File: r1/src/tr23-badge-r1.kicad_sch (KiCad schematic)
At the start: 60 parts, among them Q1 MMBT3904-TP, Q2 MMBT3904-TP, Q3 MMBT3904-TP, Y1 32.768kHz

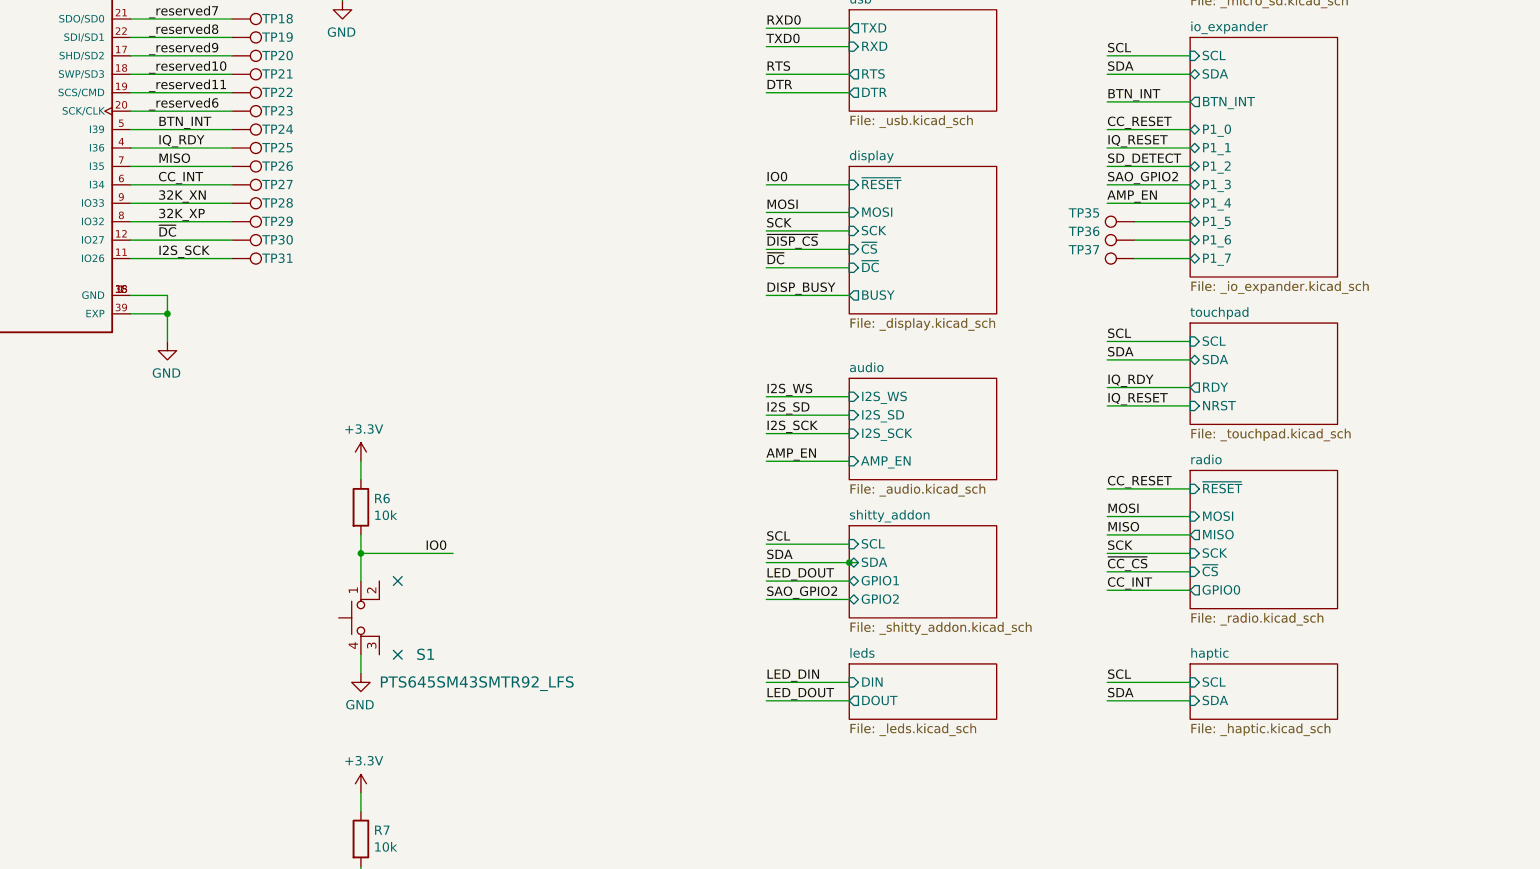
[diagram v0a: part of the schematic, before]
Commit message: Delete haptic and touchpad modules
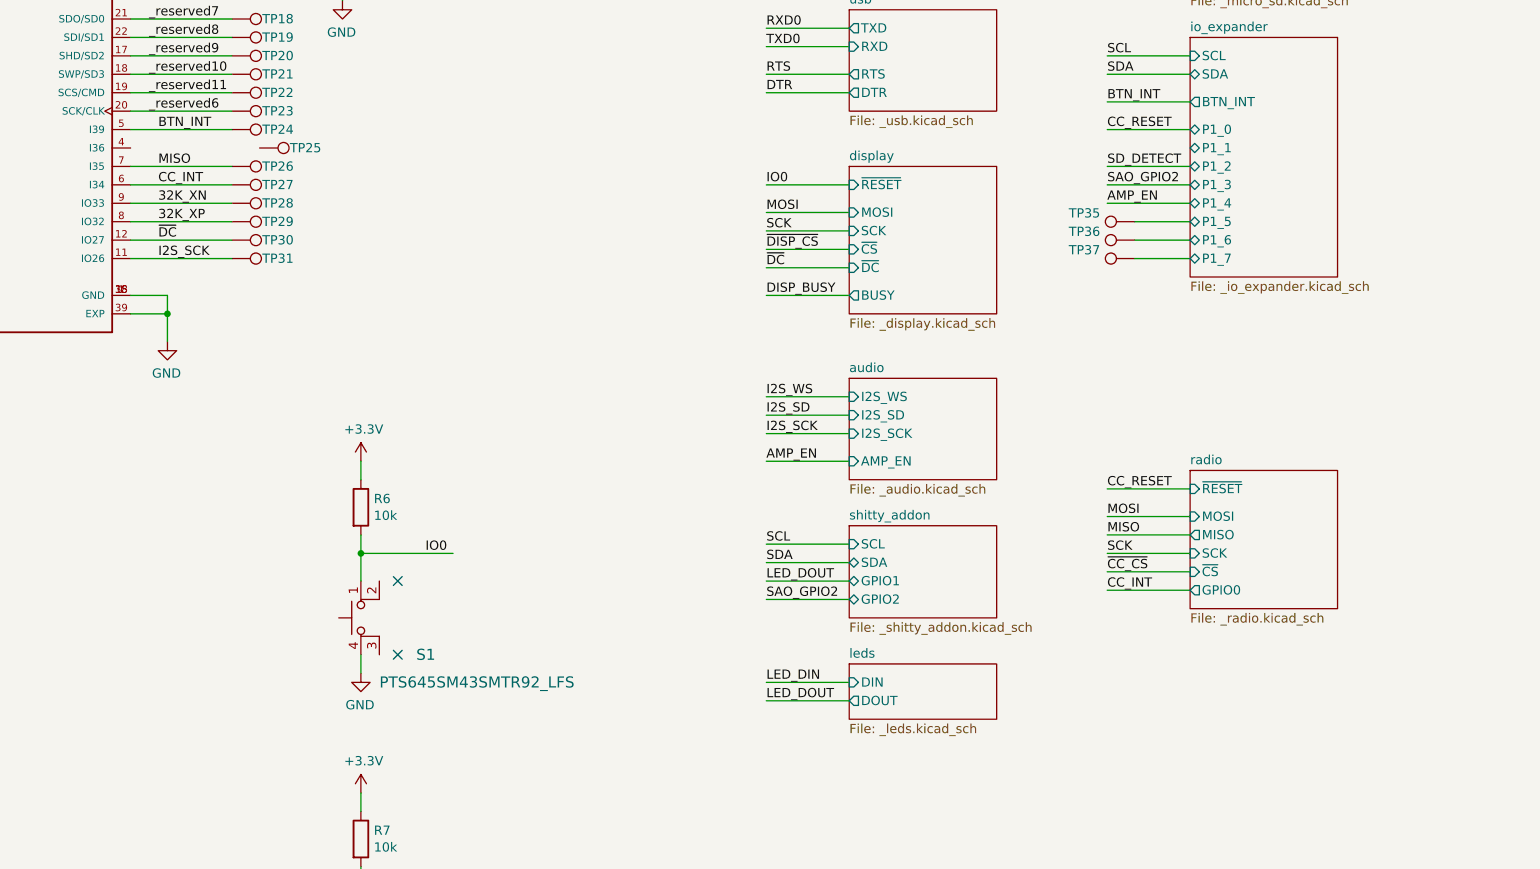
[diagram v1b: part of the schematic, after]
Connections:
- net IQ_RDY: no longer names the net of A1.4 (I36)
- net IQ_RDY: no longer TP25.1
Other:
- removed sheet haptic
- removed sheet touchpad
- moved on the sheet: TP25
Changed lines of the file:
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@@
   (junction (at 125.73 34.29) (diameter 0) (color 0 0 0 0)
-  )
-  (junction (at 195.58 124.46) (diameter 0) (color 0 0 0 0)
   )
   (junction (at 36.83 132.08) (diameter 0) (color 0 0 0 0)
@@
     (stroke (width 0) (type default))
   )
-  (wire (pts (xy 196.85 124.46) (xy 195.58 124.46))
+  (wire (pts (xy 184.15 124.46) (xy 195.58 124.46))
     (stroke (width 0) (type default))
   )
@@
     (stroke (width 0) (type default))
   )
-  (wire (pts (xy 231.14 102.87) (xy 242.57 102.87))
-    (stroke (width 0) (type default))
-  )
   (wire (pts (xy 242.57 77.47) (xy 234.95 77.47))
     (stroke (width 0) (type default))
@@
     (stroke (width 0) (type default))
   )
-  (wire (pts (xy 242.57 140.97) (xy 231.14 140.97))
-    (stroke (width 0) (type default))
-  )
   (wire (pts (xy 231.14 38.1) (xy 242.57 38.1))
     (stroke (width 0) (type default))
@@
     (stroke (width 0) (type default))
   )
-  (wire (pts (xy 96.52 67.31) (xy 110.49 67.31))
-    (stroke (width 0) (type default))
-  )
   (wire (pts (xy 128.27 179.07) (xy 128.27 185.42))
     (stroke (width 0) (type default))
@@
     (stroke (width 0) (type default))
   )
-  (wire (pts (xy 231.14 100.33) (xy 242.57 100.33))
-    (stroke (width 0) (type default))
-  )
   (wire (pts (xy 96.52 49.53) (xy 110.49 49.53))
     (stroke (width 0) (type default))
@@
     (stroke (width 0) (type default))
   )
-  (wire (pts (xy 231.14 96.52) (xy 242.57 96.52))
-    (stroke (width 0) (type default))
-  )
   (wire (pts (xy 66.04 77.47) (xy 52.07 77.47))
     (stroke (width 0) (type default))
@@
     (stroke (width 0) (type default))
   )
-  (wire (pts (xy 242.57 93.98) (xy 231.14 93.98))
-    (stroke (width 0) (type default))
-  )
-  (wire (pts (xy 242.57 67.31) (xy 231.14 67.31))
-    (stroke (width 0) (type default))
-  )
   (wire (pts (xy 34.29 115.57) (xy 39.37 115.57))
     (stroke (width 0) (type default))
@@
     (stroke (width 0) (type default))
   )
-  (wire (pts (xy 195.58 124.46) (xy 184.15 124.46))
-    (stroke (width 0) (type default))
-  )
   (wire (pts (xy 195.58 101.6) (xy 184.15 101.6))
     (stroke (width 0) (type default))
@@
     (stroke (width 0) (type default))
   )
-  (wire (pts (xy 242.57 143.51) (xy 231.14 143.51))
-    (stroke (width 0) (type default))
-  )
   (wire (pts (xy 242.57 64.77) (xy 231.14 64.77))
     (stroke (width 0) (type default))
@@
     (effects (font (size 1.27 1.27)) (justify left bottom))
   )
-  (label "IQ_RDY" (at 100.33 67.31 0)
-    (effects (font (size 1.27 1.27)) (justify left bottom))
-  )
   (label "MOSI" (at 231.14 118.11 0)
     (effects (font (size 1.27 1.27)) (justify left bottom))
@@
     (effects (font (size 1.27 1.27)) (justify left bottom))
   )
-  (label "IQ_RESET" (at 231.14 102.87 0)
-    (effects (font (size 1.27 1.27)) (justify left bottom))
-  )
   (label "~{CC_CS}" (at 52.07 74.93 0)
     (effects (font (size 1.27 1.27)) (justify left bottom))
@@
     (effects (font (size 1.27 1.27)) (justify left bottom))
   )
-  (label "SDA" (at 231.14 143.51 0)
-    (effects (font (size 1.27 1.27)) (justify left bottom))
-  )
   (label "_reserved11" (at 99.06 59.69 0)
     (effects (font (size 1.27 1.27)) (justify left bottom))
@@
     (effects (font (size 1.27 1.27)) (justify left bottom))
   )
-  (label "SDA" (at 231.14 96.52 0)
-    (effects (font (size 1.27 1.27)) (justify left bottom))
-  )
   (label "SCL" (at 184.15 121.92 0)
     (effects (font (size 1.27 1.27)) (justify left bottom))
@@
     (effects (font (size 1.27 1.27)) (justify left bottom))
   )
-  (label "IQ_RDY" (at 231.14 100.33 0)
-    (effects (font (size 1.27 1.27)) (justify left bottom))
-  )
   (label "SCK" (at 52.07 69.85 0)
     (effects (font (size 1.27 1.27)) (justify left bottom))
@@
     (effects (font (size 1.27 1.27)) (justify left bottom))
   )
-  (label "SCL" (at 231.14 140.97 0)
-    (effects (font (size 1.27 1.27)) (justify left bottom))
-  )
   (label "AMP_EN" (at 231.14 74.93 0)
     (effects (font (size 1.27 1.27)) (justify left bottom))
@@
     (effects (font (size 1.27 1.27)) (justify left bottom))
   )
-  (label "SCL" (at 231.14 93.98 0)
-    (effects (font (size 1.27 1.27)) (justify left bottom))
-  )
   (label "SCL" (at 52.07 57.15 0)
     (effects (font (size 1.27 1.27)) (justify left bottom))
@@
   )
   (label "I2S_WS" (at 52.07 59.69 0)
-    (effects (font (size 1.27 1.27)) (justify left bottom))
-  )
-  (label "IQ_RESET" (at 231.14 67.31 0)
     (effects (font (size 1.27 1.27)) (justify left bottom))
   )
@@
     )
   )
-  (symbol (lib_id "Connector:TestPoint") (at 110.49 67.31 270) (unit 1)
-    (in_bom yes) (on_board yes) (dnp no)
-    (property "Reference" "TP25" (at 116.84 67.31 90)
-      (effects (font (size 1.27 1.27)))
-    )
-    (property "Value" "~" (at 112.3696 69.9516 90)
-      (effects (font (size 1.27 1.27)) hide)
-    )
-    (property "Footprint" "jeffmakes-footprints:test-pad-1.4-TH" (at 110.49 72.39 0)
-      (effects (font (size 1.27 1.27)) hide)
-    )
-    (property "Datasheet" "~" (at 110.49 72.39 0)
+  (symbol (lib_id "Connector:TestPoint") (at 114.3 67.31 270) (unit 1)
+    (in_bom yes) (on_board yes) (dnp no)
+    (property "Reference" "TP25" (at 120.65 67.31 90)
+      (effects (font (size 1.27 1.27)))
+    )
+    (property "Value" "~" (at 116.1796 69.9516 90)
+      (effects (font (size 1.27 1.27)) hide)
+    )
+    (property "Footprint" "jeffmakes-footprints:test-pad-1.4-TH" (at 114.3 72.39 0)
+      (effects (font (size 1.27 1.27)) hide)
+    )
+    (property "Datasheet" "~" (at 114.3 72.39 0)
       (effects (font (size 1.27 1.27)) hide)
     )
@@
     )
   )
-  (sheet (at 242.57 138.43) (size 20.32 7.62) (fields_autoplaced)
-    (stroke (width 0) (type solid))
-    (fill (color 0 0 0 0.0000))
-    (property "Sheetname" "haptic" (at 242.57 137.7184 0)
-      (effects (font (size 1.27 1.27)) (justify left bottom))
-    )
-    (property "Sheetfile" "_haptic.kicad_sch" (at 242.57 146.6346 0)
-      (effects (font (size 1.27 1.27)) (justify left top))
-    )
-    (pin "SDA" input (at 242.57 143.51 180)
-      (effects (font (size 1.27 1.27)) (justify left))
-    )
-    (pin "SCL" input (at 242.57 140.97 180)
-      (effects (font (size 1.27 1.27)) (justify left))
-    )
-    (instances
-      (project "tr23-badge-r1"
-        (path "/ab725fe7-4504-40ef-b6af-82d065d00fb6" (page "12"))
-      )
-    )
-  )
   (sheet (at 242.57 33.02) (size 20.32 12.7) (fields_autoplaced)
     (stroke (width 0) (type solid))
@@
       )
     )
-  )
-  (sheet (at 242.57 91.44) (size 20.32 13.97) (fields_autoplaced)
-    (stroke (width 0) (type solid))
-    (fill (color 0 0 0 0.0000))
-    (property "Sheetname" "touchpad" (at 242.57 90.7284 0)
-      (effects (font (size 1.27 1.27)) (justify left bottom))
-    )
-    (property "Sheetfile" "_touchpad.kicad_sch" (at 242.57 105.9946 0)
-      (effects (font (size 1.27 1.27)) (justify left top))
-    )
-    (pin "SDA" bidirectional (at 242.57 96.52 180)
-      (effects (font (size 1.27 1.27)) (justify left))
-    )
-    (pin "SCL" input (at 242.57 93.98 180)
-      (effects (font (size 1.27 1.27)) (justify left))
-    )
-    (pin "RDY" output (at 242.57 100.33 180)
-      (effects (font (size 1.27 1.27)) (justify left))
-    )
-    (pin "NRST" input (at 242.57 102.87 180)
-      (effects (font (size 1.27 1.27)) (justify left))
-    )
-    (instances
-      (project "tr23-badge-r1"
-        (path "/ab725fe7-4504-40ef-b6af-82d065d00fb6" (page "10"))
-      )
-    )

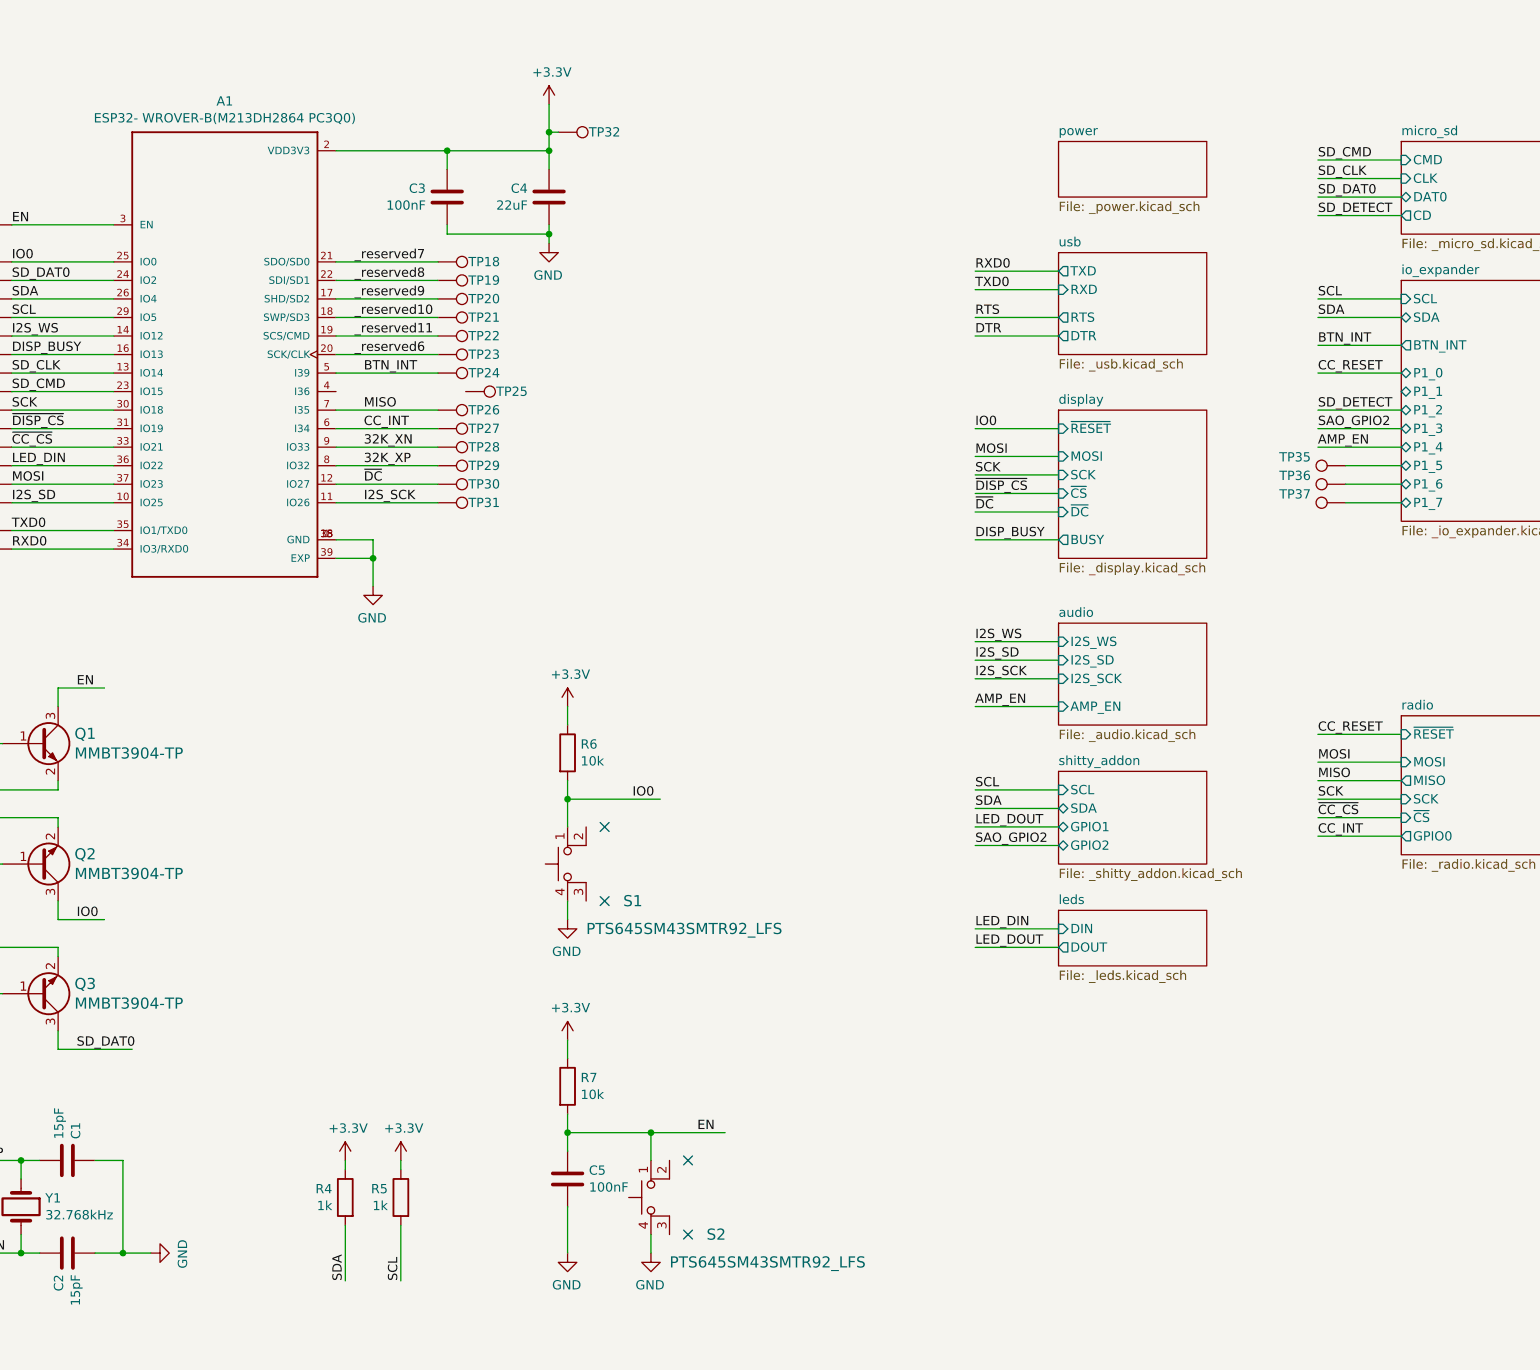
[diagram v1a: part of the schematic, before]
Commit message: Update all symbols
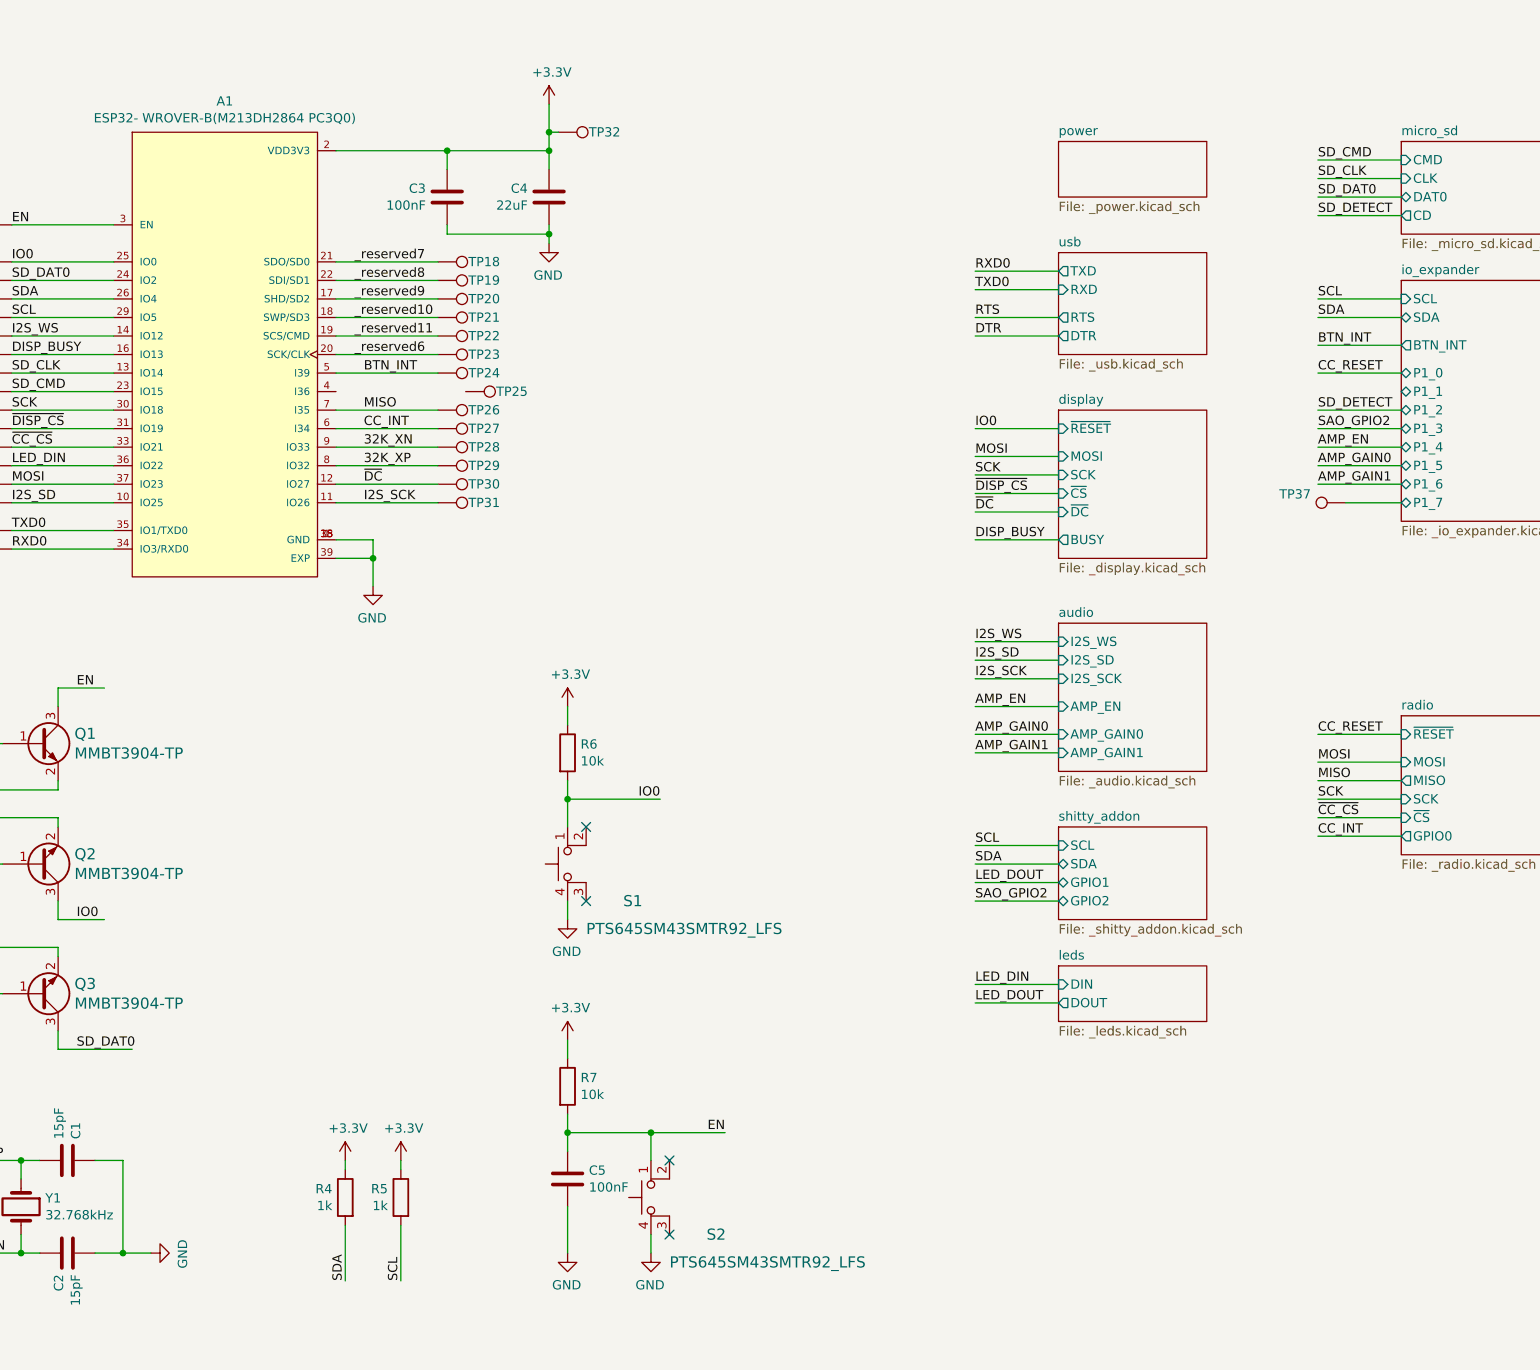
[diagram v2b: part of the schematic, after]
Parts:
- removed TP35, TP36: ~, TestPoint:TestPoint_Pad_D1.0mm, symbol Connector:TestPoint
- A1: footprint jeffmakes-footprints:ESP32-WROVER-I -> XCVR_ESP32-WROVER-I
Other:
- sheet audio ports: added AMP_GAIN0, AMP_GAIN1; removed none

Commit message: Backlight connection
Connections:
- net IO0: no longer A1.25 (IO0), R6.2, S1.1, TP2.1
- net BACKLIGHT: now reaches A1.4 (I36)
- net BACKLIGHT: now also TP25.1
- net BTN_INT renamed KEY_INT
- net DISP_BUSY renamed FSYNC
- new net ~{RESET}: A1.25 (IO0), R6.2, S1.1, TP2.1
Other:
- added sheet keyboard (_keyboard.kicad_sch)
- sheet display ports: added BACKLIGHT, CS, DC, FMARK; removed BUSY, ~{CS}, ~{DC}
- sheet io_expander ports: added INT; removed BTN_INT
- note added: "Pin routing: In the ESP32, any digital periphal signal can be routed to any IO pad. 18 pads have optional RTC/analog functionality."
- moved on the sheet: TP25
